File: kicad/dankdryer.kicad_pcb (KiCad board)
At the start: 2 copper layers, 100 x 75 mm, 43 parts, among them J1 Barreljack, J2 upper fan, J3 lower fan, J4 heater, J5 Screw_Terminal_01x04, J7 5kg load cell, J8 motor, J9 Conn_01x04, Q1 BT136S-800E, Q2 SSM3K127TU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

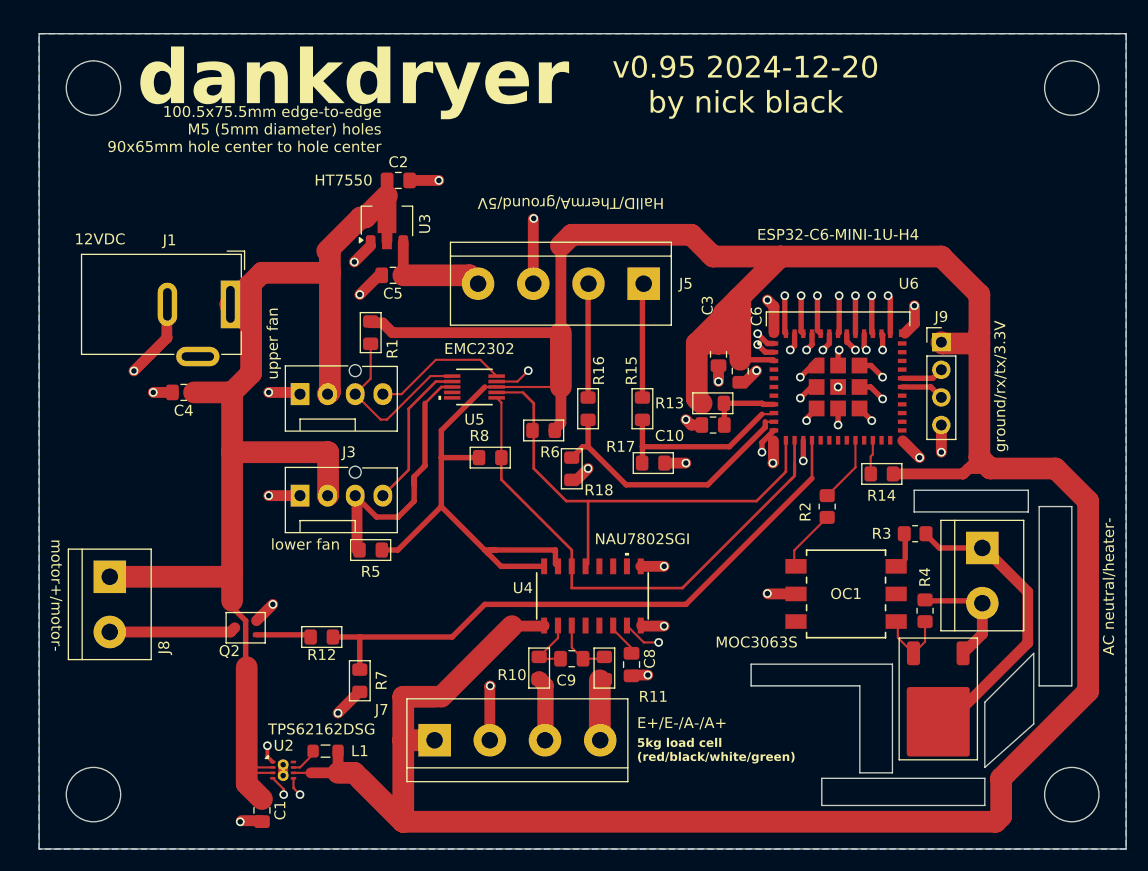
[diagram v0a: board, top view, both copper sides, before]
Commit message: kicad: mention U.FL connector
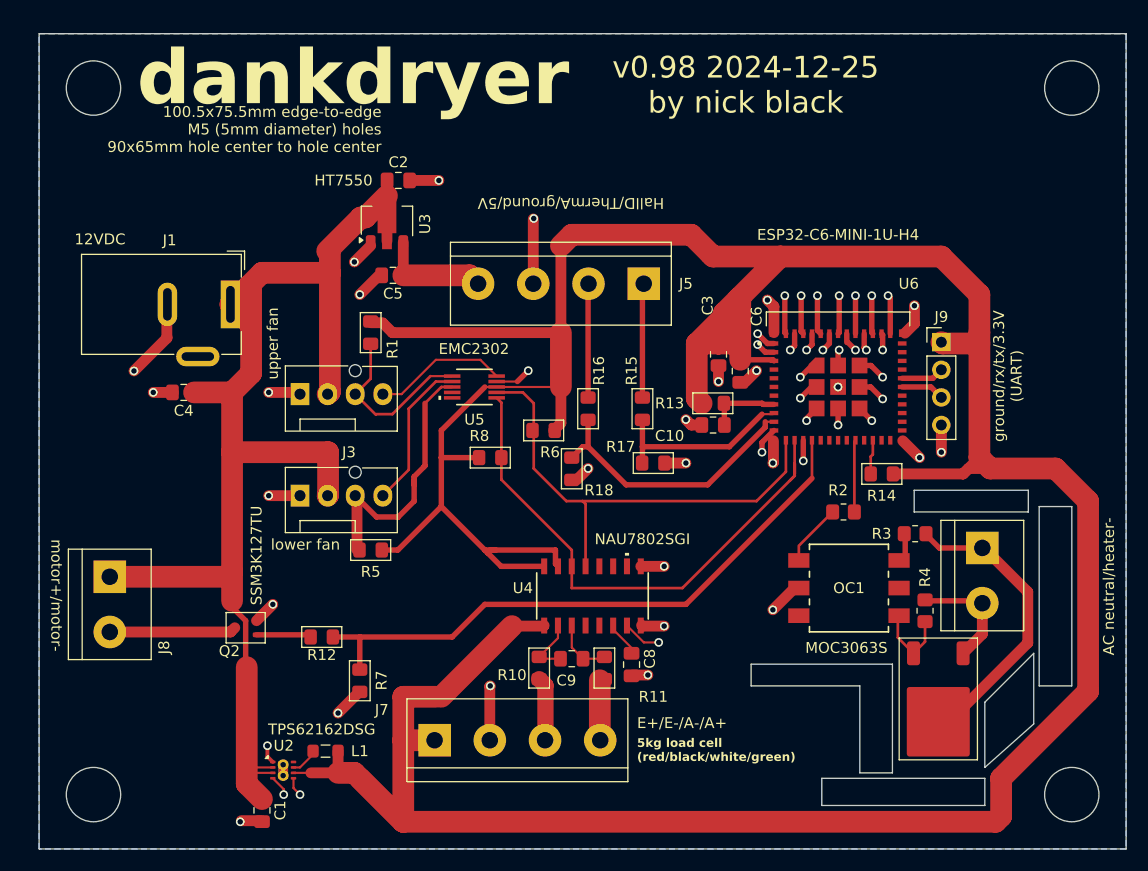
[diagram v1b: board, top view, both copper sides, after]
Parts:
- moved R2 1.58 mm to (124.0, 94.0), turned to 0 degrees
- moved OC1 0.60 mm to (124.5, 101.0)
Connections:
- net /Hot chamber microboard/AH3712QAnalog renamed /Hot chamber microboard/HallAnalog
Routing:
- net Net-(OC1-A): track 5.76 -> 5.04 mm
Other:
- board text added: "ground/rx/tx/3.3V (UART)"
- board text added: "v0.98 2024-12-25 by nick black"
- board text removed: "ground/rx/tx/3.3V"
- board text removed: "v0.95 2024-12-20 by nick black"

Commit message: kicad: note about AVDD on NAU7802
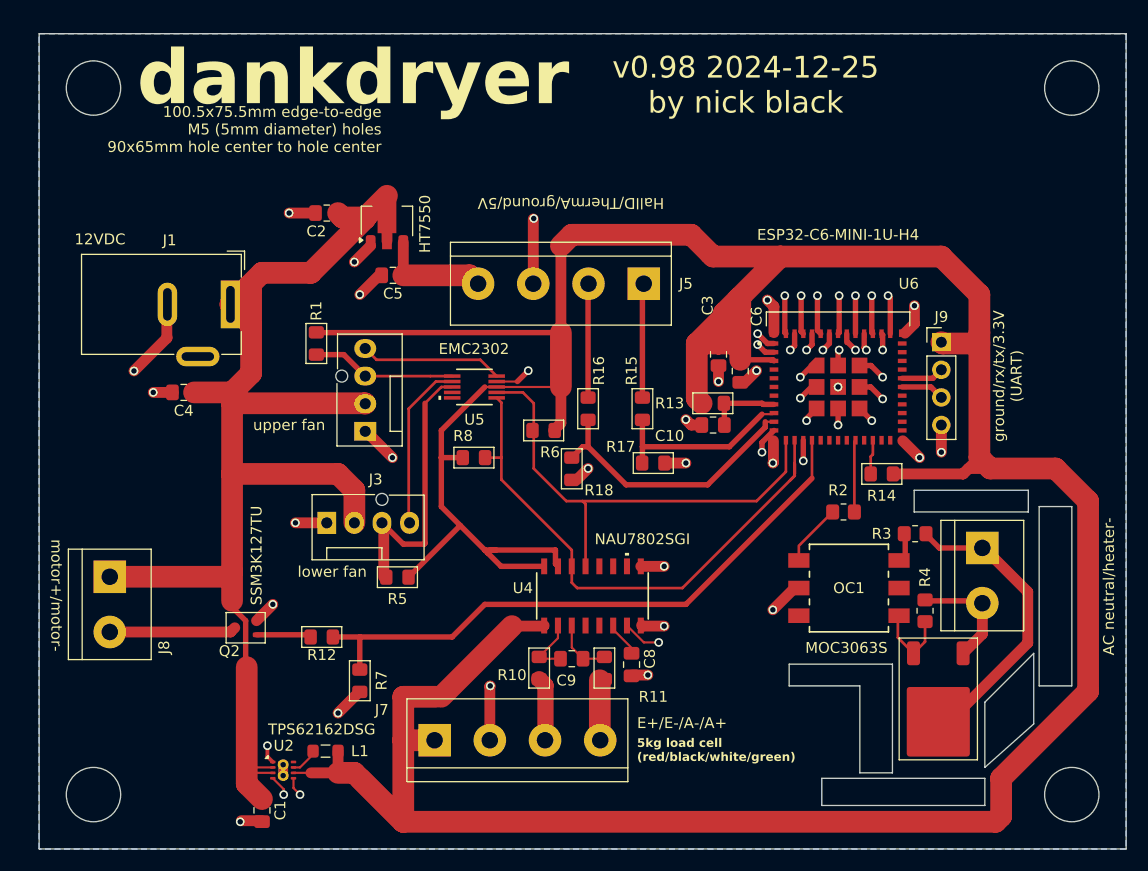
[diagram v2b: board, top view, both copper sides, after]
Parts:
- moved C2 7.24 mm to (76.5, 66.5), turned to 180 degrees
- moved J2 6.91 mm to (80.0, 86.6), turned to 90 degrees
- moved R1 5.10 mm to (75.5, 78.5)
- moved J3 3.51 mm to (76.5, 95.0)
- moved R5 3.51 mm to (83.0, 100.0)
- moved R8 1.50 mm to (90.0, 89.0)
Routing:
- net +12V: track 120.1 -> 123.5 mm
- net Net-(J2-Pin_3): track 16.4 -> 13.3 mm
- net +3.3V: track 339.3 -> 342.0 mm
- net Net-(J3-Pin_4): track 14.0 -> 15.5 mm
- net /SDA: track 50.4 -> 51.6 mm
- net Net-(J2-Pin_4): track 12.4 -> 13.1 mm
- net Net-(J3-Pin_3): track 25.0 -> 25.6 mm
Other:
- outline, holes or cut-outs redrawn

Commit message: kicad: pcb v0.99
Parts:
- removed Q1: BT136S-800E, PCM_Package_TO_SOT_SMD_AKL:TO-252-2
- added Q3: T1210-800G, PCM_Package_TO_SOT_SMD_AKL:TO-263-2, F.Cu at (132.1, 100.3)
- moved J4 16.9 mm to (134.0, 114.0), turned to 180 degrees
- moved OC1 8.75 mm to (117.0, 105.5)
- moved R3 8.23 mm to (122.5, 97.5), turned to 90 degrees
- moved R4 5.96 mm to (127.5, 107.5), turned to 0 degrees
- moved R14 5.83 mm to (133.0, 88.5)
- moved J9 1.88 mm to (133.0, 76.5)
- moved R2 1.58 mm to (122.5, 93.5), turned to 90 degrees
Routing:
- net Net-(OC1-A): track 5.04 -> 13.6 mm
- net /ACNeutral: track 10.4 -> 18.6 mm
- net +3.3V: track 342.0 -> 334.1 mm
- net /HeaterNeutral: track 27.1 -> 23.5 mm
- net Net-(U6-IO8): track 3.18 -> 6.26 mm
- net Net-(OC1-MT1): track 6.96 -> 9.85 mm
- net Net-(OC1-MT2): track 2.33 -> 4.83 mm
- net /SDA: track 51.6 -> 49.6 mm
- net GND: track 139.2 -> 140.5 mm
- net /TXD0: track 3.92 -> 4.70 mm
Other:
- outline, holes or cut-outs redrawn
- board text added: "v0.99 2024-12-26 by nick black"
- board text removed: "v0.98 2024-12-25 by nick black"

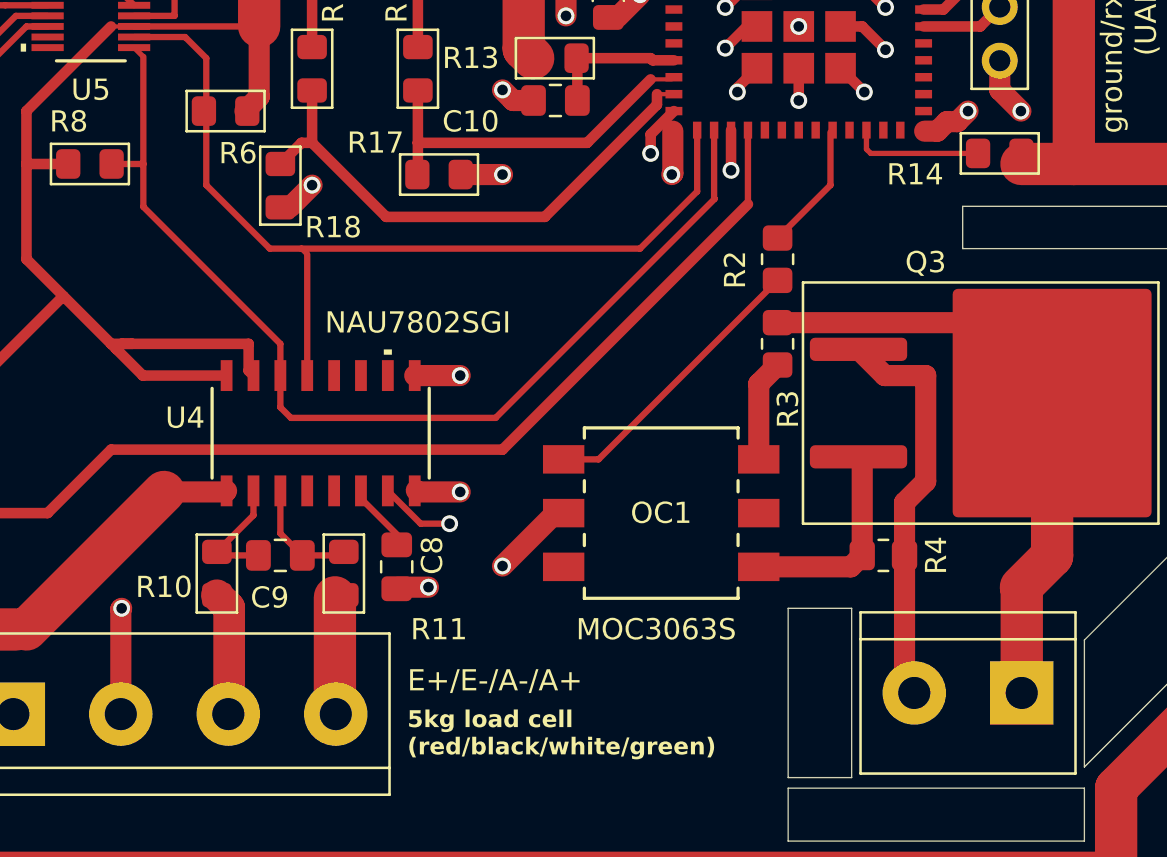
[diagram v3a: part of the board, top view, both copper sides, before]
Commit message: 470pf capacitor on VI2N + VI2P
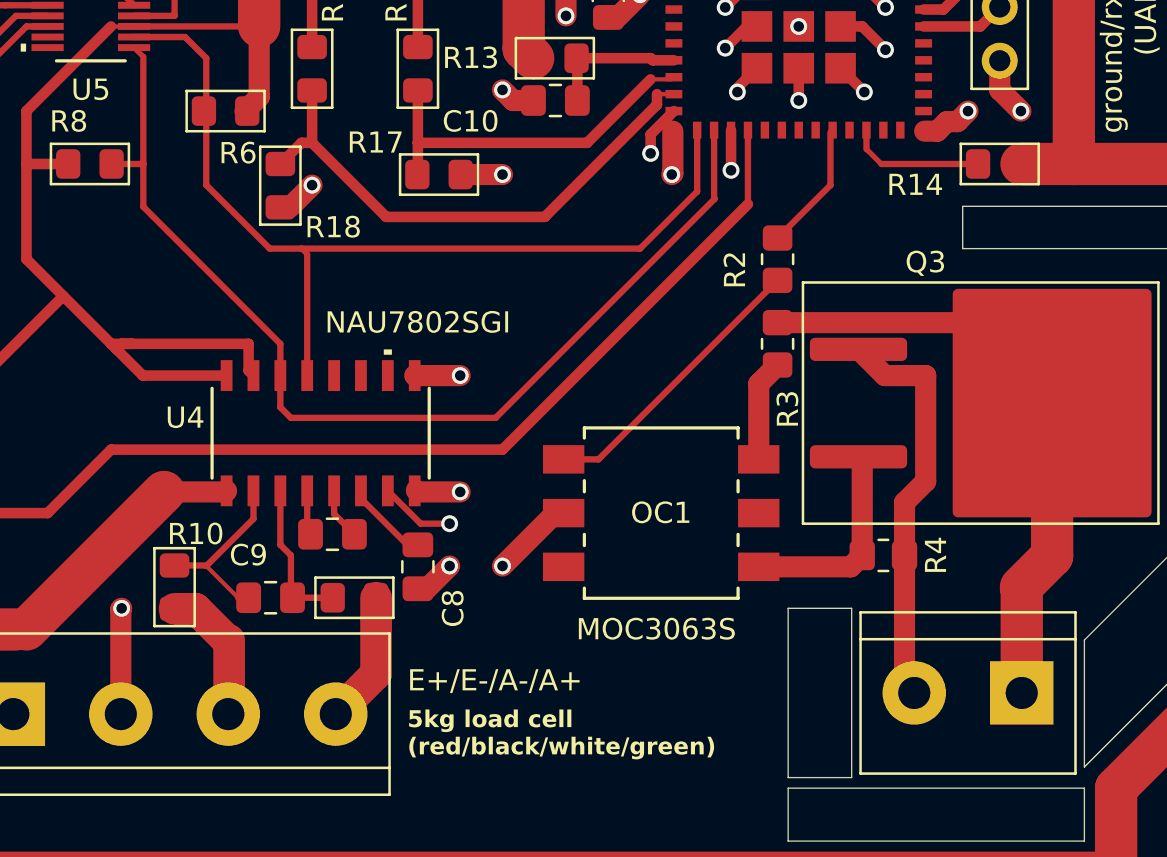
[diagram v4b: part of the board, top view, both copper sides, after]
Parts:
- added C11: 470pf, Capacitor_SMD:C_0805_2012Metric_Pad1.18x1.45mm_HandSolder, F.Cu at (101.5, 106.5)
- moved R10 2.10 mm to (94.0, 109.0)
- moved C9 2.05 mm to (98.5, 109.5)
- moved R11 1.25 mm to (102.5, 109.5), turned to 180 degrees
- moved C8 1.00 mm to (105.5, 108.0)
- moved R14 0.50 mm to (133.0, 89.0)
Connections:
- U4 pad 4: unconnected-(U4-VIN2N-Pad4) -> Net-(U4-VIN2N)
- U4 pad 5: unconnected-(U4-VIN2P-Pad5) -> Net-(U4-VIN2P)
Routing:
- net Net-(U4-VIN1N): track 5.40 -> 8.61 mm
- net Net-(U4-VIN2P): track 0.00 -> 2.45 mm
- net Net-(U4-VIN2N): track 0.00 -> 1.90 mm
- net Net-(U4-VIN1P): track 5.28 -> 7.08 mm
- net /A+: track 5.00 -> 6.29 mm
- net /A-: track 5.34 -> 6.07 mm

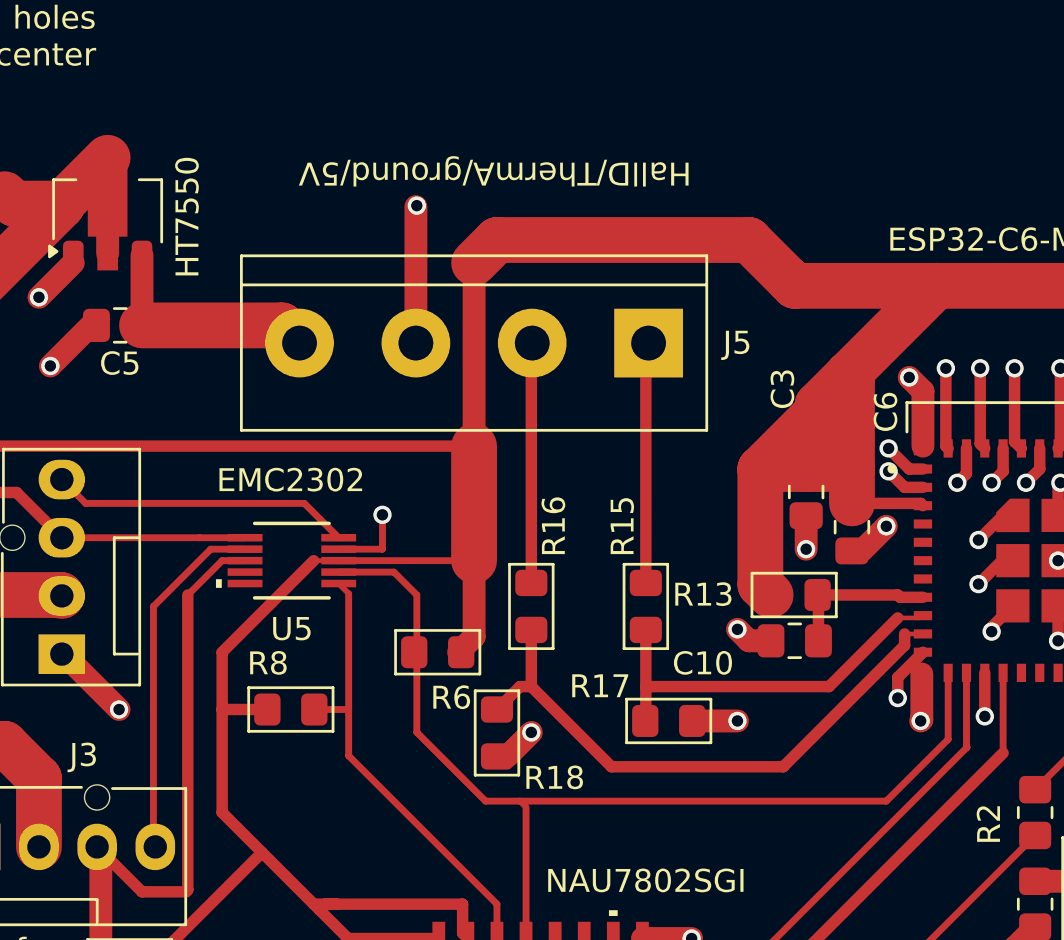
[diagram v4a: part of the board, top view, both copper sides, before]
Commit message: take 3.3V to microboard rather than dividing 5V on return from hall sensor
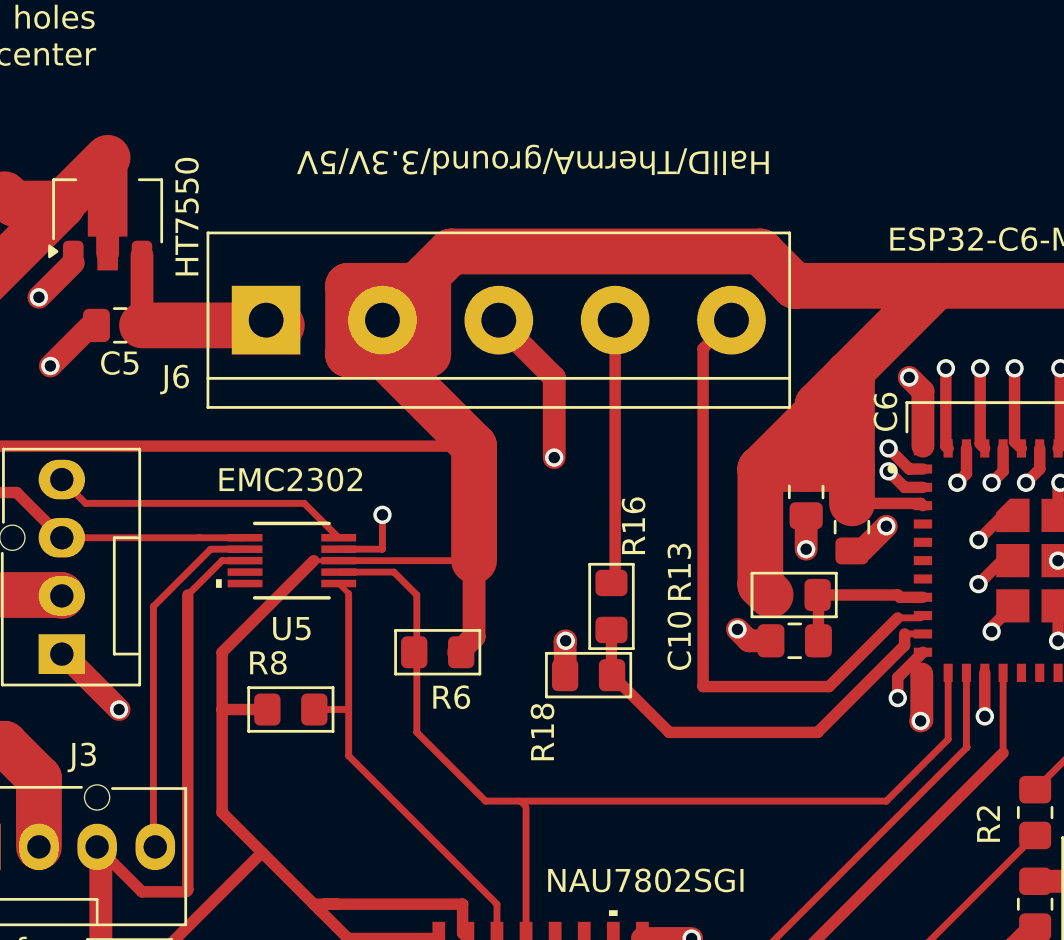
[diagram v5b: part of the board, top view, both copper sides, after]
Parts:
- removed J5: Screw_Terminal_01x04, dank:TerminalBlock_bornier-4_P5.08mm
- removed R15: 412, PCM_Resistor_SMD_AKL:R_0805_2012Metric_Pad1.15x1.40mm_HandSolder
- removed R17: 680, PCM_Resistor_SMD_AKL:R_0805_2012Metric_Pad1.15x1.40mm_HandSolder
- added J6: Screw_Terminal_01x05, dank:TerminalBlock_bornier-5_P5.08mm, F.Cu at (88.9, 72.0)
- moved R18 4.73 mm to (103.0, 87.5), turned to 0 degrees
- moved R16 3.50 mm to (104.0, 84.5)
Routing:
- net +3.3V: track 334.1 -> 349.1 mm
- net /Hot chamber microboard/HallAnalog: track 10.4 -> 0.00 mm
- net /Hall: track 17.2 -> 27.3 mm
- net /Therm: track 25.6 -> 18.6 mm
- net +5VA: track 10.2 -> 9.16 mm
- net GND: track 140.6 -> 139.5 mm, vias 57 -> 56
- net /Hot chamber microboard/ThermAnalog: track 10.4 -> 11.3 mm
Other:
- board text added: "HallD/ThermA/ground/3.3V/5V"
- board text removed: "HallD/ThermA/ground/5V"
